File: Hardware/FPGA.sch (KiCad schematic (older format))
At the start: 4 parts

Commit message: Getting down structure, some components created.
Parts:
- removed U? (x4): ICE40UP5K-SG48ITR, Package_DFN_QFN:QFN-48-1EP_7x7mm_P0.5mm_EP5.6x5.6mm, symbol FPGA_Lattice:ICE40UP5K-SG48ITR
- added U501: ICE40UP5K-SG48, tomu-fpga:QFN-48-1EP_7x7mm_P0.5mm_EP5.6x5.6mm, symbol pkl_lattice:ICE40UP5K-SG48
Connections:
- net labels added: LED_B, LED_G, LED_R
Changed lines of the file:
@@
 $EndDescr
 $Comp
-L FPGA_Lattice:ICE40UP5K-SG48ITR U?
-U 1 1 6121B3F0
-P 4200 2800
-F 0 "U?" H 4530 2853 50  0000 L CNN
-F 1 "ICE40UP5K-SG48ITR" H 4530 2762 50  0000 L CNN
-F 2 "Package_DFN_QFN:QFN-48-1EP_7x7mm_P0.5mm_EP5.6x5.6mm" H 4200 1450 50  0001 C CNN
-F 3 "http://www.latticesemi.com/Products/FPGAandCPLD/iCE40Ultra" H 3800 3800 50  0001 C CNN
-	1    4200 2800
+L pkl_lattice:ICE40UP5K-SG48 U501
+U 1 1 61224EB1
+P 6450 3150
+F 0 "U501" H 6450 5315 50  0000 C CNN
+F 1 "ICE40UP5K-SG48" H 6450 5224 50  0000 C CNN
+F 2 "tomu-fpga:QFN-48-1EP_7x7mm_P0.5mm_EP5.6x5.6mm" H 8750 3350 50  0001 C CNN
+F 3 "" H 8750 3350 50  0001 C CNN
+	1    6450 3150
 	1    0    0    -1
 $EndComp
-$Comp
-L FPGA_Lattice:ICE40UP5K-SG48ITR U?
-U 2 1 6121C11C
-P 6200 2850
-F 0 "U?" H 6200 1775 50  0000 C CNN
-F 1 "ICE40UP5K-SG48ITR" H 6200 1684 50  0000 C CNN
-F 2 "Package_DFN_QFN:QFN-48-1EP_7x7mm_P0.5mm_EP5.6x5.6mm" H 6200 1500 50  0001 C CNN
-F 3 "http://www.latticesemi.com/Products/FPGAandCPLD/iCE40Ultra" H 5800 3850 50  0001 C CNN
-	2    6200 2850
-	1    0    0    -1
-$EndComp
-$Comp
-L FPGA_Lattice:ICE40UP5K-SG48ITR U?
-U 3 1 6121CDD3
-P 7600 4600
-F 0 "U?" H 7930 4703 50  0000 L CNN
-F 1 "ICE40UP5K-SG48ITR" H 7930 4612 50  0000 L CNN
-F 2 "Package_DFN_QFN:QFN-48-1EP_7x7mm_P0.5mm_EP5.6x5.6mm" H 7600 3250 50  0001 C CNN
-F 3 "http://www.latticesemi.com/Products/FPGAandCPLD/iCE40Ultra" H 7200 5600 50  0001 C CNN
-	3    7600 4600
-	1    0    0    -1
-$EndComp
-$Comp
-L FPGA_Lattice:ICE40UP5K-SG48ITR U?
-U 4 1 6121D881
-P 5450 5350
-F 0 "U?" H 5680 5396 50  0000 L CNN
-F 1 "ICE40UP5K-SG48ITR" H 5680 5305 50  0000 L CNN
-F 2 "Package_DFN_QFN:QFN-48-1EP_7x7mm_P0.5mm_EP5.6x5.6mm" H 5450 4000 50  0001 C CNN
-F 3 "http://www.latticesemi.com/Products/FPGAandCPLD/iCE40Ultra" H 5050 6350 50  0001 C CNN
-	4    5450 5350
-	1    0    0    -1
-$EndComp
+Text HLabel 7450 3050 2    50   Output ~ 0
+LED_B
+Text HLabel 7450 2850 2    50   Output ~ 0
+LED_G
+Text HLabel 7450 2950 2    50   Output ~ 0
+LED_R
 $EndSCHEMATC

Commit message: Checking in some libraries.
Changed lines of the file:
@@
 	1    0    0    -1
 $EndComp
-Text HLabel 7450 3050 2    50   Output ~ 0
+Text HLabel 7550 3050 2    50   Output ~ 0
 LED_B
-Text HLabel 7450 2850 2    50   Output ~ 0
+Text HLabel 7550 2850 2    50   Output ~ 0
 LED_G
-Text HLabel 7450 2950 2    50   Output ~ 0
+Text HLabel 7550 2950 2    50   Output ~ 0
 LED_R
+Wire Wire Line
+	7450 2850 7550 2850
+Wire Wire Line
+	7450 2950 7550 2950
+Wire Wire Line
+	7450 3050 7550 3050
 $EndSCHEMATC

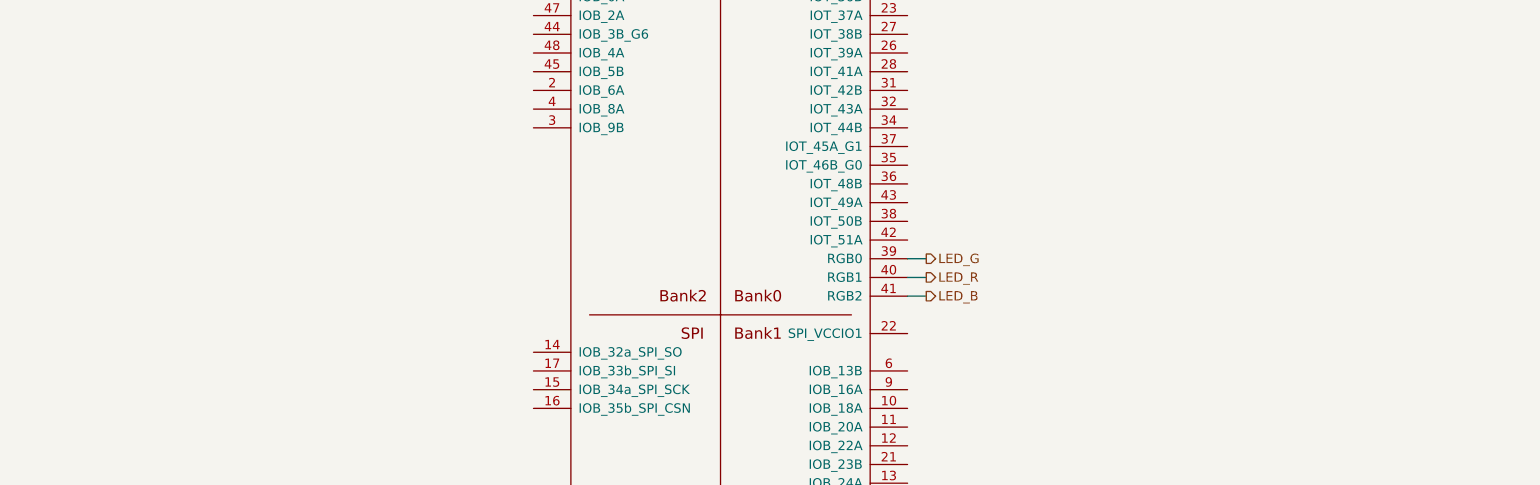
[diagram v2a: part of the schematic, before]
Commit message: Moving some components around.
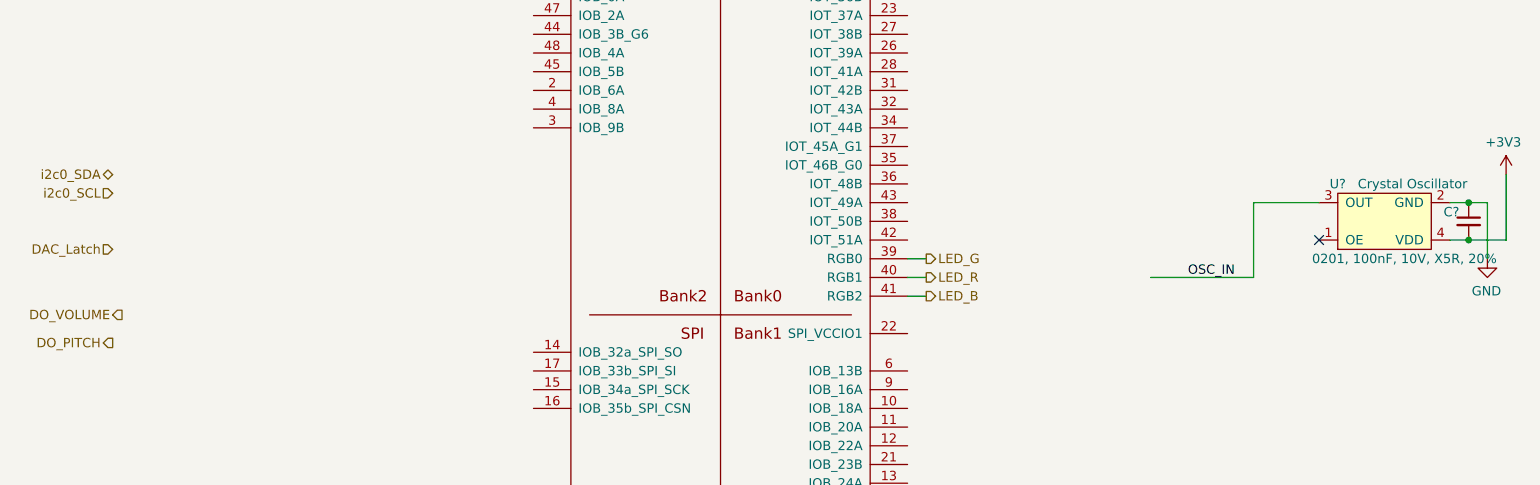
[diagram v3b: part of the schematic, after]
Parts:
- added C?: 0201, 100nF, 10V, X5R, 20%, tomu-fpga:C_0201_0603Metric, symbol Device:C_Small
- added U?: Crystal Oscillator, tomu-fpga:XTAL-2520, symbol tomu-fpga:Oscillator
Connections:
- net labels added: +3V3, DAC_Latch, DO_PITCH, DO_VOLUME, GND, OSC_IN, i2c0_SCL, i2c0_SDA
- wire segments 3 -> 12
- no-connect marks 0 -> 1
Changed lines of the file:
@@
 Wire Wire Line
 	7450 3050 7550 3050
+Text HLabel 3200 2400 0    50   BiDi ~ 0
+i2c0_SDA
+Text HLabel 3200 2500 0    50   Input ~ 0
+i2c0_SCL
+Text HLabel 3200 2800 0    50   Input ~ 0
+DAC_Latch
+Text HLabel 3250 3150 0    50   Output ~ 0
+DO_VOLUME
+Text HLabel 3200 3300 0    50   Output ~ 0
+DO_PITCH
+NoConn ~ 9650 2750
+Wire Wire Line
+	9300 2950 9300 2550
+Wire Wire Line
+	10650 2400 10650 2750
+Wire Wire Line
+	8750 2950 9300 2950
+Text Label 9200 2950 2    50   ~ 0
+OSC_IN
+Wire Wire Line
+	9650 2550 9300 2550
+Wire Wire Line
+	10450 2750 10350 2750
+Wire Wire Line
+	10450 2550 10550 2550
+$Comp
+L Device:C_Small C?
+U 1 1 614FF0DF
+P 10450 2650
+F 0 "C?" H 10500 2700 50  0000 L CNN
+F 1 "0201, 100nF, 10V, X5R, 20%" H 10300 2450 50  0000 L CNN
+F 2 "tomu-fpga:C_0201_0603Metric" H 10450 2650 50  0001 C CNN
+F 3 "" H 10450 2650 50  0001 C CNN
+F 4 "ANY" H 5400 550 50  0001 C CNN "MPN"
+F 5 "ANY" H 5400 550 50  0001 C CNN "MYPN"
+F 6 "ANY" H 5400 550 50  0001 C CNN "Manufacturer"
+F 7 "C" H 10450 2650 50  0001 C CNN "Spice_Primitive"
+F 8 "100n" H 10450 2650 50  0001 C CNN "Spice_Model"
+F 9 "Y" H 10450 2650 50  0001 C CNN "Spice_Netlist_Enabled"
+	1    10450 2650
+	-1   0    0    -1
+$EndComp
+Wire Wire Line
+	10550 2550 10550 2850
+$Comp
+L power:GND #PWR?
+U 1 1 614FF0E6
+P 10550 2850
+F 0 "#PWR?" H 10550 2600 50  0001 C CNN
+F 1 "GND" H 10555 2677 50  0000 C CNN
+F 2 "" H 10550 2850 50  0001 C CNN
+F 3 "" H 10550 2850 50  0001 C CNN
+	1    10550 2850
+	-1   0    0    -1
+$EndComp
+Connection ~ 10450 2550
+Wire Wire Line
+	10350 2550 10450 2550
+Connection ~ 10450 2750
+Wire Wire Line
+	10650 2750 10450 2750
+$Comp
+L power:+3V3 #PWR?
+U 1 1 614FF0F0
+P 10650 2400
+F 0 "#PWR?" H 10650 2250 50  0001 C CNN
+F 1 "+3V3" H 10665 2573 50  0000 C CNN
+F 2 "" H 10650 2400 50  0001 C CNN
+F 3 "" H 10650 2400 50  0001 C CNN
+	1    10650 2400
+	-1   0    0    -1
+$EndComp
+$Comp
+L tomu-fpga:Oscillator U?
+U 1 1 614FF0FA
+P 10000 2500
+F 0 "U?" H 9750 2450 50  0000 C CNN
+F 1 "Crystal Oscillator" H 10150 2450 50  0000 C CNN
+F 2 "tomu-fpga:XTAL-2520" H 10000 2500 50  0001 C CNN
+F 3 "https://www.ecsxtal.com/store/pdf/ECS-2520MV.pdf" H 10000 2500 50  0001 C CNN
+F 4 "XC2756CT-ND" H 10000 2500 50  0001 C CNN "MPN"
+F 5 "ECS" H 10000 2500 50  0001 C CNN "Manufacturer"
+F 6 "XC2756CT-ND" H 10000 2500 50  0001 C CNN "DPN"
+F 7 "XTAL OSC XO 48.0000MHZ CMOS SMD" H 5200 150 50  0001 C CNN "Description"
+	1    10000 2500
+	1    0    0    1
+$EndComp
 $EndSCHEMATC

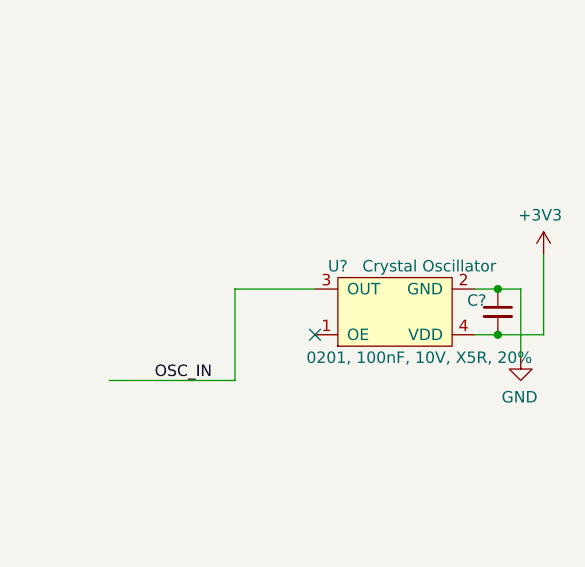
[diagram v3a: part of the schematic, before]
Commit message: Adding libraries for TRRS.
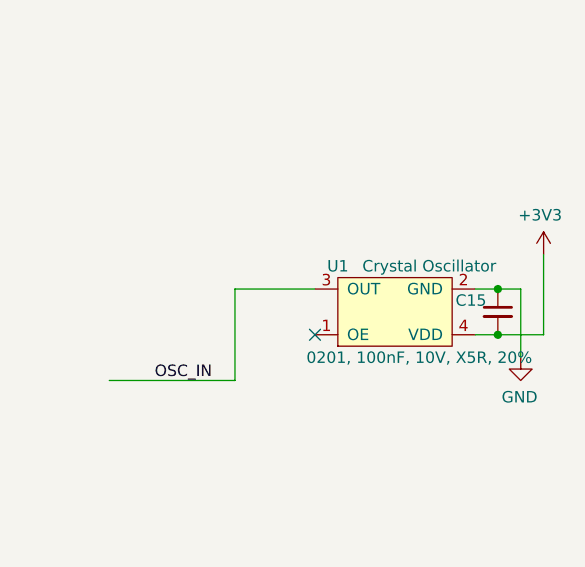
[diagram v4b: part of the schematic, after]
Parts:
- gave numbers to parts that had none: 2
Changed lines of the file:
@@
 	10450 2550 10550 2550
 $Comp
-L Device:C_Small C?
+L Device:C_Small C15
 U 1 1 614FF0DF
 P 10450 2650
-F 0 "C?" H 10500 2700 50  0000 L CNN
+F 0 "C15" H 10500 2700 50  0000 L CNN
 F 1 "0201, 100nF, 10V, X5R, 20%" H 10300 2450 50  0000 L CNN
 F 2 "tomu-fpga:C_0201_0603Metric" H 10450 2650 50  0001 C CNN
@@
 	10550 2550 10550 2850
 $Comp
-L power:GND #PWR?
+L power:GND #PWR0102
 U 1 1 614FF0E6
 P 10550 2850
-F 0 "#PWR?" H 10550 2600 50  0001 C CNN
+F 0 "#PWR0102" H 10550 2600 50  0001 C CNN
 F 1 "GND" H 10555 2677 50  0000 C CNN
 F 2 "" H 10550 2850 50  0001 C CNN
@@
 	10650 2750 10450 2750
 $Comp
-L power:+3V3 #PWR?
+L power:+3V3 #PWR0103
 U 1 1 614FF0F0
 P 10650 2400
-F 0 "#PWR?" H 10650 2250 50  0001 C CNN
+F 0 "#PWR0103" H 10650 2250 50  0001 C CNN
 F 1 "+3V3" H 10665 2573 50  0000 C CNN
 F 2 "" H 10650 2400 50  0001 C CNN
@@
 $EndComp
 $Comp
-L tomu-fpga:Oscillator U?
+L tomu-fpga:Oscillator U1
 U 1 1 614FF0FA
 P 10000 2500
-F 0 "U?" H 9750 2450 50  0000 C CNN
+F 0 "U1" H 9750 2450 50  0000 C CNN
 F 1 "Crystal Oscillator" H 10150 2450 50  0000 C CNN
 F 2 "tomu-fpga:XTAL-2520" H 10000 2500 50  0001 C CNN

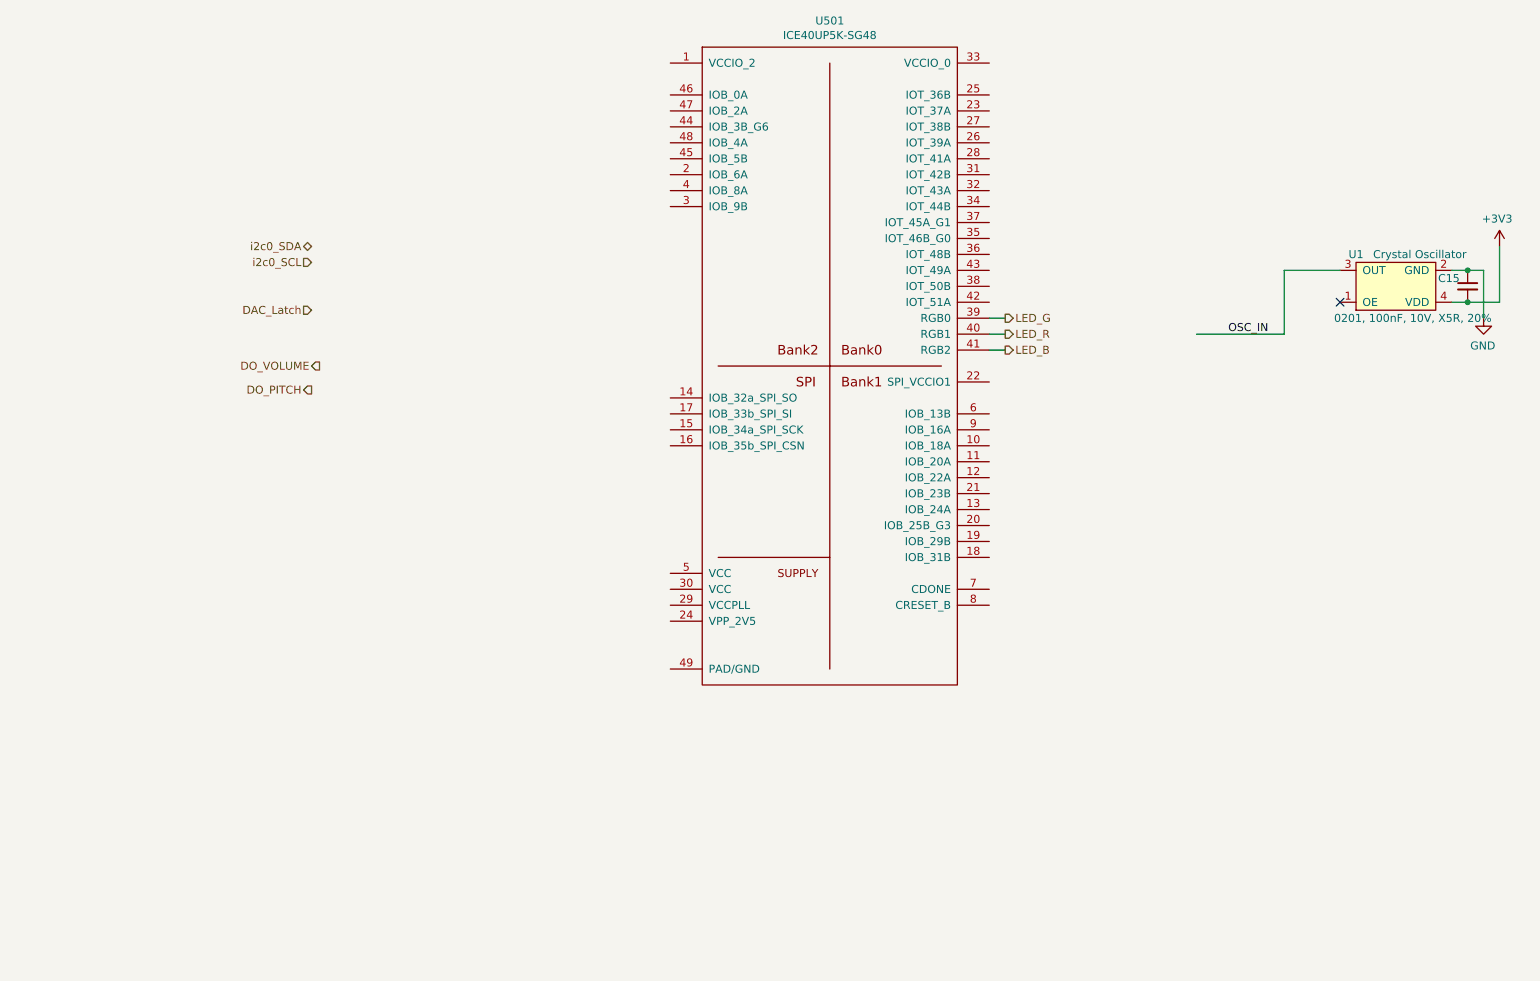
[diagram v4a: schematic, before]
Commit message: Cleaning up a few associations, changing 0805 to 0603 footprints on AFE.
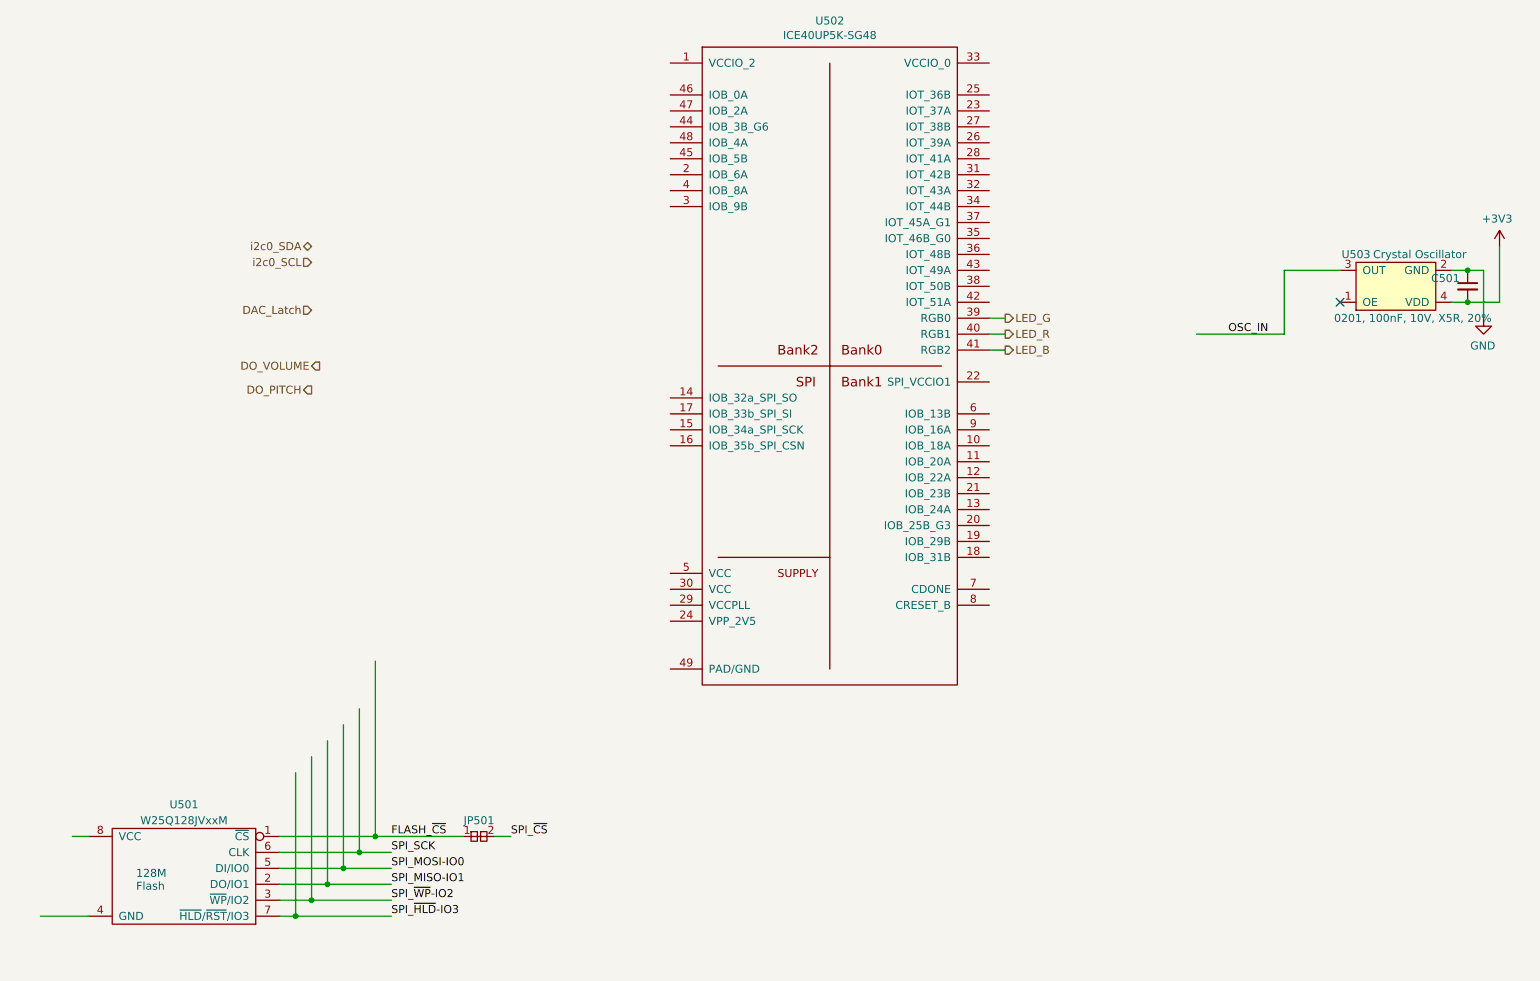
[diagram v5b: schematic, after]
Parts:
- added JP501: Jumper, pkl_jumpers:J_NC_0402_15, symbol pkl_misc:pkl_jumper_nc
- added U501: W25Q128JVxxM, Package_SON:WSON-8-1EP_6x5mm_P1.27mm_EP3.4x4.3mm, symbol pkl_memory:W25Q
- renumbered C15 to C501, U501 to U502, U1 to U503
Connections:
- net labels added: FLASH_~CS, SPI_MISO-IO1, SPI_MOSI-IO0, SPI_SCK, SPI_~CS, SPI_~HLD~-IO3, SPI_~WP~-IO2
- wire segments 12 -> 33
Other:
- note added: "128M\nFlash"
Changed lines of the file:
@@
 $Descr A4 11693 8268
 encoding utf-8
-Sheet 5 8
+Sheet 5 9
 Title ""
 Date ""
@@
 $EndDescr
 $Comp
-L pkl_lattice:ICE40UP5K-SG48 U501
+L pkl_lattice:ICE40UP5K-SG48 U502
 U 1 1 61224EB1
 P 6450 3150
-F 0 "U501" H 6450 5315 50  0000 C CNN
+F 0 "U502" H 6450 5315 50  0000 C CNN
 F 1 "ICE40UP5K-SG48" H 6450 5224 50  0000 C CNN
 F 2 "tomu-fpga:QFN-48-1EP_7x7mm_P0.5mm_EP5.6x5.6mm" H 8750 3350 50  0001 C CNN
@@
 	10450 2550 10550 2550
 $Comp
-L Device:C_Small C15
+L Device:C_Small C501
 U 1 1 614FF0DF
 P 10450 2650
-F 0 "C15" H 10500 2700 50  0000 L CNN
+F 0 "C501" H 10500 2700 50  0000 L CNN
 F 1 "0201, 100nF, 10V, X5R, 20%" H 10300 2450 50  0000 L CNN
 F 2 "tomu-fpga:C_0201_0603Metric" H 10450 2650 50  0001 C CNN
@@
 	10550 2550 10550 2850
 $Comp
-L power:GND #PWR0102
+L power:GND #PWR0501
 U 1 1 614FF0E6
 P 10550 2850
-F 0 "#PWR0102" H 10550 2600 50  0001 C CNN
+F 0 "#PWR0501" H 10550 2600 50  0001 C CNN
 F 1 "GND" H 10555 2677 50  0000 C CNN
 F 2 "" H 10550 2850 50  0001 C CNN
@@
 	10650 2750 10450 2750
 $Comp
-L power:+3V3 #PWR0103
+L power:+3V3 #PWR0502
 U 1 1 614FF0F0
 P 10650 2400
-F 0 "#PWR0103" H 10650 2250 50  0001 C CNN
+F 0 "#PWR0502" H 10650 2250 50  0001 C CNN
 F 1 "+3V3" H 10665 2573 50  0000 C CNN
 F 2 "" H 10650 2400 50  0001 C CNN
@@
 $EndComp
 $Comp
-L tomu-fpga:Oscillator U1
+L tomu-fpga:Oscillator U503
 U 1 1 614FF0FA
 P 10000 2500
-F 0 "U1" H 9750 2450 50  0000 C CNN
+F 0 "U503" H 9750 2450 50  0000 C CNN
 F 1 "Crystal Oscillator" H 10150 2450 50  0000 C CNN
 F 2 "tomu-fpga:XTAL-2520" H 10000 2500 50  0001 C CNN
@@
 	1    0    0    1
 $EndComp
+Text Label 4450 6100 0    50   ~ 0
+SPI_~CS
+Text Label 3700 6200 0    50   ~ 0
+SPI_SCK
+Text Label 3700 6300 0    50   ~ 0
+SPI_MOSI-IO0
+Text Label 3700 6400 0    50   ~ 0
+SPI_MISO-IO1
+Text Label 3700 6500 0    50   ~ 0
+SPI_~WP~-IO2
+Text Label 3700 6600 0    50   ~ 0
+SPI_~HLD~-IO3
+Wire Wire Line
+	3000 6400 3300 6400
+Wire Wire Line
+	3000 6300 3400 6300
+$Comp
+L pkl_misc:pkl_jumper_nc JP?
+U 1 1 612A0D70
+P 4250 6100
+AR Path="/61291C71/612A0D70" Ref="JP?"  Part="1"
+AR Path="/611E3335/612A0D70" Ref="JP501"  Part="1"
+F 0 "JP501" H 4250 6200 50  0000 C CNN
+F 1 "Jumper" H 4250 6245 60  0001 C CNN
+F 2 "pkl_jumpers:J_NC_0402_15" H 4250 6100 60  0001 C CNN
+F 3 "" H 4250 6100 60  0000 C CNN
+F 4 "ANY" H 4250 6100 50  0001 C CNN "Source"
+	1    4250 6100
+	1    0    0    -1
+$EndComp
+Wire Wire Line
+	3000 6100 3600 6100
+Wire Wire Line
+	3000 6200 3500 6200
+Wire Wire Line
+	3000 6500 3200 6500
+Wire Wire Line
+	3000 6600 3100 6600
+Wire Wire Line
+	3100 5700 3100 6600
+Connection ~ 3100 6600
+Wire Wire Line
+	3200 5600 3200 6500
+Connection ~ 3200 6500
+Wire Wire Line
+	3500 5300 3500 6200
+Connection ~ 3500 6200
+Wire Wire Line
+	3600 5000 3600 6100
+Wire Wire Line
+	3600 6100 4150 6100
+Wire Wire Line
+	3400 5400 3400 6300
+Connection ~ 3400 6300
+Wire Wire Line
+	3300 5500 3300 6400
+Connection ~ 3300 6400
+Text Label 3700 6100 0    50   ~ 0
+FLASH_~CS
+Wire Wire Line
+	3500 6200 3700 6200
+Wire Wire Line
+	4350 6100 4450 6100
+Wire Wire Line
+	3400 6300 3700 6300
+Wire Wire Line
+	3300 6400 3700 6400
+Wire Wire Line
+	3200 6500 3700 6500
+Wire Wire Line
+	3100 6600 3700 6600
+Connection ~ 3600 6100
+Wire Wire Line
+	1500 6600 1800 6600
+Wire Wire Line
+	1700 6100 1800 6100
+Text Notes 2100 6450 0    50   ~ 0
+128M\nFlash
+$Comp
+L pkl_memory:W25Q U?
+U 1 1 612A0D93
+P 2400 6300
+AR Path="/61291C71/612A0D93" Ref="U?"  Part="1"
+AR Path="/611E3335/612A0D93" Ref="U501"  Part="1"
+F 0 "U501" H 2400 6700 50  0000 C CNN
+F 1 "W25Q128JVxxM" H 2400 6600 50  0000 C CNN
+F 2 "Package_SON:WSON-8-1EP_6x5mm_P1.27mm_EP3.4x4.3mm" H 2400 6300 50  0001 C CNN
+F 3 "" H 2400 6300 50  0001 C CNN
+F 4 "ANY" H 2400 6300 50  0001 C CNN "Source"
+F 5 "eeprom-wson8-w25q128" H -5500 -1650 50  0001 C CNN "Key"
+F 6 "W25Q128JVPIM TR" H 2400 6300 50  0001 C CNN "MPN"
+F 7 "W25Q128JVPIMCT-ND" H 2400 6300 50  0001 C CNN "DPN"
+	1    2400 6300
+	-1   0    0    -1
+$EndComp
 $EndSCHEMATC

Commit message: Checking in bits.
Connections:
- net labels added: VO_PITCH, VO_VOLUME
- net labels removed: DO_PITCH, DO_VOLUME
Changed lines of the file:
@@
 DAC_Latch
 Text HLabel 3250 3150 0    50   Output ~ 0
-DO_VOLUME
+VO_VOLUME
 Text HLabel 3200 3300 0    50   Output ~ 0
-DO_PITCH
+VO_PITCH
 NoConn ~ 9650 2750
 Wire Wire Line
